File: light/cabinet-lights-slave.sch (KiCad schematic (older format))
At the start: 14 parts, among them J1 CONN_01x03, J2 CONN_01x03, J3 CONN_01x03, J4 CONN_01x03, Q1 Q_PMOS_GDS, U1 MCP6001

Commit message: More schematic wrangling
Parts for light module
Initial PCB for light module
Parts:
- removed D1, D2, D3: LED, symbol LED
- removed Q1: Q_PMOS_GDS, symbol Q_PMOS_GDS
- removed R3, R4: R, symbol R
- removed U1: MCP6001, symbol MCP6001
- added D1, D2, D3: XLAMP-MX-3, parts:XLAMP-MX-3, symbol XLAMP-MX-3
- added HS1: HEATSINK, parts:25mm_heatsink, symbol TESTPAD
- added OP?1: MIC6211, agg:SOT-23-5, symbol MIC6211
- added Q1: NX7002AK, agg:SOT-23, symbol Q_NMOS_GSD
- added Q2: NTR1P02T1G, agg:SOT-23, symbol Q_PMOS_GSD
- added R6: 1k, agg:0603, symbol R
- J1: value CONN_01x03 -> NORTH; footprint (none) -> parts:S3D-XH-A; Farnell (none) -> 1516290
- J2: value CONN_01x03 -> EAST; footprint (none) -> parts:S3D-XH-A; Farnell (none) -> 1516290
- J3: value CONN_01x03 -> SOUTH; footprint (none) -> parts:S3D-XH-A; Farnell (none) -> 1516290
- J4: value CONN_01x03 -> WEST; footprint (none) -> parts:S3D-XH-A; Farnell (none) -> 1516290
- R1: value 9k -> 9k9; footprint (none) -> agg:0603
- R2: value 1k -> 100R; footprint (none) -> agg:0603
- R5: value R -> 0R24; footprint (none) -> agg:0603; Farnell (none) -> 2328092
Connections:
- net labels added: DIM/100
- net labels removed: DIM/10
- wire segments 22 -> 23

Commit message: Models for LED and JST conn, slight PCB shuffle
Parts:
- J1, J2, J3, J4: footprint parts:S3D-XH-A -> parts:S3B-XH-A
- renumbered R5 to R3, R6 to R4
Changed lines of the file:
@@
 F 0 "J1" H 4231 2673 50  0001 C CNN
 F 1 "NORTH" V 4100 2450 50  0000 C CNN
-F 2 "parts:S3D-XH-A" H 4200 2550 50  0001 C CNN
+F 2 "parts:S3B-XH-A" H 4200 2550 50  0001 C CNN
 F 3 "http://www.farnell.com/datasheets/5448.pdf" H 4200 2550 50  0001 C CNN
 F 4 "1516290" H 4200 2550 60  0001 C CNN "Farnell"
@@
 $EndComp
 $Comp
-L R R5
+L R R3
 U 1 1 577A3D2F
 P 6400 3625
-F 0 "R5" H 6470 3671 50  0001 L CNN
+F 0 "R3" H 6470 3671 50  0001 L CNN
 F 1 "0R24" V 6400 3625 50  0000 C CNN
 F 2 "agg:0603" V 6330 3625 50  0001 C CNN
@@
 $EndComp
 $Comp
-L R R6
+L R R4
 U 1 1 577B9A14
 P 6100 2500
-F 0 "R6" V 5893 2500 50  0001 C CNN
+F 0 "R4" V 5893 2500 50  0001 C CNN
 F 1 "1k" V 6100 2500 50  0000 C CNN
 F 2 "agg:0603" V 6030 2500 50  0001 C CNN
@@
 F 0 "J2" H 4231 3023 50  0001 C CNN
 F 1 "EAST" V 4100 2800 50  0000 C CNN
-F 2 "parts:S3D-XH-A" H 4200 2900 50  0001 C CNN
+F 2 "parts:S3B-XH-A" H 4200 2900 50  0001 C CNN
 F 3 "http://www.farnell.com/datasheets/5448.pdf" H 4200 2900 50  0001 C CNN
 F 4 "1516290" H 4200 2900 60  0001 C CNN "Farnell"
@@
 F 0 "J3" H 4231 3373 50  0001 C CNN
 F 1 "SOUTH" V 4100 3150 50  0000 C CNN
-F 2 "parts:S3D-XH-A" H 4200 3250 50  0001 C CNN
+F 2 "parts:S3B-XH-A" H 4200 3250 50  0001 C CNN
 F 3 "http://www.farnell.com/datasheets/5448.pdf" H 4200 3250 50  0001 C CNN
 F 4 "1516290" H 4200 3250 60  0001 C CNN "Farnell"
@@
 F 0 "J4" H 4231 3723 50  0001 C CNN
 F 1 "WEST" V 4100 3500 50  0000 C CNN
-F 2 "parts:S3D-XH-A" H 4200 3600 50  0001 C CNN
+F 2 "parts:S3B-XH-A" H 4200 3600 50  0001 C CNN
 F 3 "http://www.farnell.com/datasheets/5448.pdf" H 4200 3600 50  0001 C CNN
 F 4 "1516290" H 4200 3600 60  0001 C CNN "Farnell"

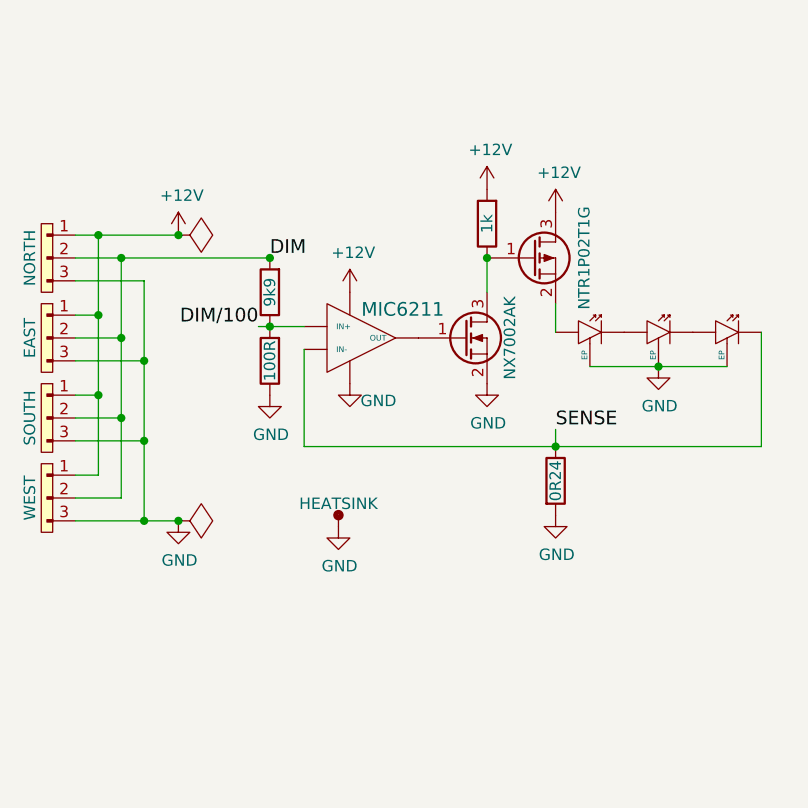
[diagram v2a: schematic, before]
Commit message: Tweak to use BJT transistor
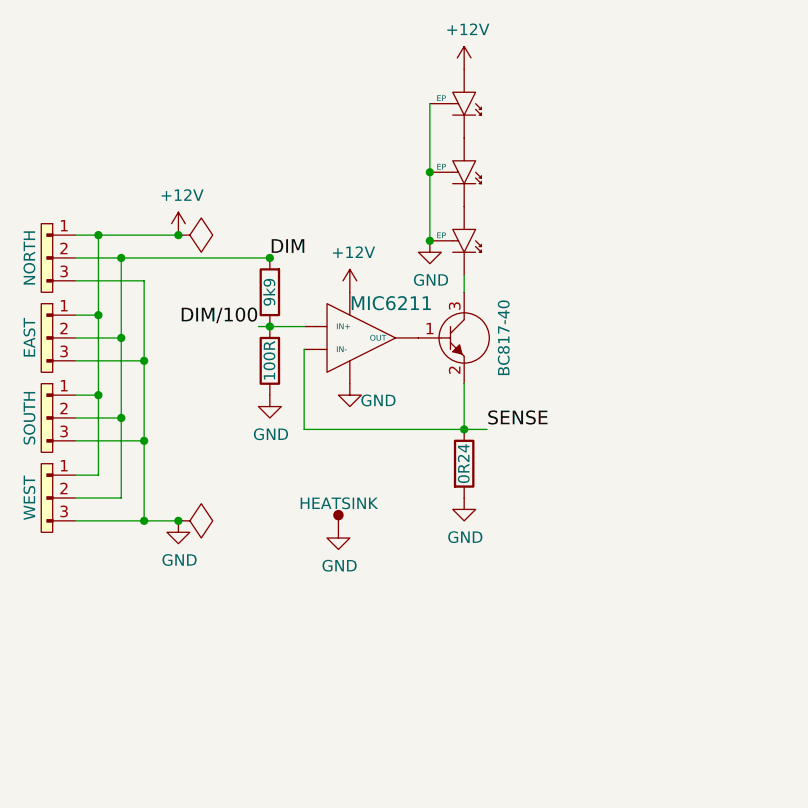
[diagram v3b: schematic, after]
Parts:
- removed Q1: NX7002AK, agg:SOT-23, symbol Q_NMOS_GSD
- removed Q2: NTR1P02T1G, agg:SOT-23, symbol Q_PMOS_GSD
- removed R4: 1k, agg:0603, symbol R
- added Q1: BC817-40, agg:SOT-23, symbol NPN
- renumbered OP?1 to OP1
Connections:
- net +12V: now also D1.2
- net SENSE: now also Q1.2 (E); no longer D3.1
- net at OP1.1 (OUT): now also Q1.1 (B)
- new net: D3.1, Q1.3 (C)
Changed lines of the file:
@@
 $EndComp
 $Comp
-L +12V #PWR01
+L +12V #PWR1
 U 1 1 577A3A01
 P 4750 2550
-F 0 "#PWR01" H 4750 2400 50  0001 C CNN
+F 0 "#PWR1" H 4750 2400 50  0001 C CNN
 F 1 "+12V" H 4765 2723 50  0000 C CNN
 F 2 "" H 4750 2550 50  0000 C CNN
@@
 $EndComp
 $Comp
-L PWR_FLAG #FLG02
+L PWR_FLAG #FLG1
 U 1 1 577A3A92
 P 4750 2550
-F 0 "#FLG02" H 4750 2645 50  0001 C CNN
+F 0 "#FLG1" H 4750 2645 50  0001 C CNN
 F 1 "PWR_FLAG" V 4750 2728 50  0001 L CNN
 F 2 "" H 4750 2550 50  0000 C CNN
@@
 $EndComp
 $Comp
-L +12V #PWR03
+L +12V #PWR5
 U 1 1 577A3BB5
 P 5500 2800
-F 0 "#PWR03" H 5500 2650 50  0001 C CNN
+F 0 "#PWR5" H 5500 2650 50  0001 C CNN
 F 1 "+12V" H 5515 2973 50  0000 C CNN
 F 2 "" H 5500 2800 50  0000 C CNN
@@
 $EndComp
 $Comp
-L GND #PWR04
+L GND #PWR6
 U 1 1 577A3BC0
 P 5500 3200
-F 0 "#PWR04" H 5500 2950 50  0001 C CNN
+F 0 "#PWR6" H 5500 2950 50  0001 C CNN
 F 1 "GND" H 5625 3125 50  0000 C CNN
 F 2 "" H 5500 3200 50  0000 C CNN
@@
 L R R3
 U 1 1 577A3D2F
-P 6400 3625
-F 0 "R3" H 6470 3671 50  0001 L CNN
-F 1 "0R24" V 6400 3625 50  0000 C CNN
-F 2 "agg:0603" V 6330 3625 50  0001 C CNN
-F 3 "http://www.farnell.com/datasheets/2004190.pdf" H 6400 3625 50  0001 C CNN
-F 4 "2328092" H 6400 3625 60  0001 C CNN "Farnell"
-	1    6400 3625
-	1    0    0    -1
-$EndComp
-$Comp
-L +12V #PWR05
+P 6000 3550
+F 0 "R3" H 6070 3596 50  0001 L CNN
+F 1 "0R24" V 6000 3550 50  0000 C CNN
+F 2 "agg:0603" V 5930 3550 50  0001 C CNN
+F 3 "http://www.farnell.com/datasheets/2004190.pdf" H 6000 3550 50  0001 C CNN
+F 4 "2328092" H 6000 3550 60  0001 C CNN "Farnell"
+	1    6000 3550
+	1    0    0    -1
+$EndComp
+$Comp
+L +12V #PWR8
 U 1 1 577A3FBE
-P 6400 2450
-F 0 "#PWR05" H 6400 2300 50  0001 C CNN
-F 1 "+12V" H 6415 2623 50  0000 C CNN
-F 2 "" H 6400 2450 50  0000 C CNN
-F 3 "" H 6400 2450 50  0000 C CNN
-	1    6400 2450
-	1    0    0    -1
-$EndComp
-$Comp
-L GND #PWR06
+P 6000 1825
+F 0 "#PWR8" H 6000 1675 50  0001 C CNN
+F 1 "+12V" H 6015 1998 50  0000 C CNN
+F 2 "" H 6000 1825 50  0000 C CNN
+F 3 "" H 6000 1825 50  0000 C CNN
+	1    6000 1825
+	1    0    0    -1
+$EndComp
+$Comp
+L GND #PWR9
 U 1 1 577A3FD8
-P 6400 3775
-F 0 "#PWR06" H 6400 3525 50  0001 C CNN
-F 1 "GND" H 6405 3602 50  0000 C CNN
-F 2 "" H 6400 3775 50  0000 C CNN
-F 3 "" H 6400 3775 50  0000 C CNN
-	1    6400 3775
+P 6000 3700
+F 0 "#PWR9" H 6000 3450 50  0001 C CNN
+F 1 "GND" H 6005 3527 50  0000 C CNN
+F 2 "" H 6000 3700 50  0000 C CNN
+F 3 "" H 6000 3700 50  0000 C CNN
+	1    6000 3700
 	1    0    0    -1
 $EndComp
@@
 	4300 3800 4750 3800
 $Comp
-L GND #PWR07
+L GND #PWR2
 U 1 1 577A3A2D
 P 4750 3800
-F 0 "#PWR07" H 4750 3550 50  0001 C CNN
+F 0 "#PWR2" H 4750 3550 50  0001 C CNN
 F 1 "GND" H 4755 3627 50  0000 C CNN
 F 2 "" H 4750 3800 50  0000 C CNN
@@
 $EndComp
 $Comp
-L PWR_FLAG #FLG08
+L PWR_FLAG #FLG2
 U 1 1 577A3AA4
 P 4750 3800
-F 0 "#FLG08" H 4750 3895 50  0001 C CNN
+F 0 "#FLG2" H 4750 3895 50  0001 C CNN
 F 1 "PWR_FLAG" V 4750 3978 50  0001 L CNN
 F 2 "" H 4750 3800 50  0000 C CNN
@@
 $EndComp
 $Comp
-L GND #PWR09
+L GND #PWR3
 U 1 1 577A5F6E
 P 5150 3250
-F 0 "#PWR09" H 5150 3000 50  0001 C CNN
+F 0 "#PWR3" H 5150 3000 50  0001 C CNN
 F 1 "GND" H 5155 3077 50  0000 C CNN
 F 2 "" H 5150 3250 50  0000 C CNN
@@
 Connection ~ 5150 2950
 Connection ~ 5150 2650
-Text Label 6400 3400 0    60   ~ 0
+Text Label 6100 3400 0    60   ~ 0
 SENSE
-Connection ~ 6400 3475
-$Comp
-L GND #PWR010
-U 1 1 577B9A09
-P 6100 3200
-F 0 "#PWR010" H 6100 2950 50  0001 C CNN
-F 1 "GND" H 6105 3027 50  0000 C CNN
-F 2 "" H 6100 3200 50  0000 C CNN
-F 3 "" H 6100 3200 50  0000 C CNN
-	1    6100 3200
-	1    0    0    -1
-$EndComp
-$Comp
-L R R4
-U 1 1 577B9A14
-P 6100 2500
-F 0 "R4" V 5893 2500 50  0001 C CNN
-F 1 "1k" V 6100 2500 50  0000 C CNN
-F 2 "agg:0603" V 6030 2500 50  0001 C CNN
-F 3 "" H 6100 2500 50  0000 C CNN
-	1    6100 2500
-	-1   0    0    1
-$EndComp
-$Comp
-L +12V #PWR011
-U 1 1 577B9A1F
-P 6100 2350
-F 0 "#PWR011" H 6100 2200 50  0001 C CNN
-F 1 "+12V" H 6115 2523 50  0000 C CNN
-F 2 "" H 6100 2350 50  0000 C CNN
-F 3 "" H 6100 2350 50  0000 C CNN
-	1    6100 2350
-	1    0    0    -1
-$EndComp
-$Comp
-L Q_PMOS_GSD Q2
-U 1 1 577B9E2C
-P 6300 2650
-F 0 "Q2" H 6491 2696 50  0001 L CNN
-F 1 "NTR1P02T1G" V 6525 2650 50  0000 C CNN
-F 2 "agg:SOT-23" H 6500 2750 50  0001 C CNN
-F 3 "http://www.farnell.com/datasheets/1708311.pdf" H 6300 2650 50  0001 C CNN
-F 4 "2317617" H 6300 2650 60  0001 C CNN "Farnell"
-	1    6300 2650
-	1    0    0    -1
-$EndComp
-$Comp
-L Q_NMOS_GSD Q1
-U 1 1 577BA518
-P 6000 3000
-F 0 "Q1" H 6191 3046 50  0001 L CNN
-F 1 "NX7002AK" V 6200 3000 50  0000 C CNN
-F 2 "agg:SOT-23" H 6200 3100 50  0001 C CNN
-F 3 "http://www.farnell.com/datasheets/1968065.pdf" H 6000 3000 50  0001 C CNN
-	1    6000 3000
-	1    0    0    -1
-$EndComp
-Wire Wire Line
-	6100 2800 6100 2650
-Connection ~ 6100 2650
-$Comp
-L MIC6211 OP?1
+Connection ~ 6000 3400
+$Comp
+L MIC6211 OP1
 U 1 1 577BB3FE
 P 5500 3000
-F 0 "OP?1" H 5575 2900 60  0001 L CNN
-F 1 "MIC6211" H 5550 3125 60  0000 L CNN
+F 0 "OP1" H 5575 2900 60  0001 L CNN
+F 1 "MIC6211" H 5500 3150 60  0000 L CNN
 F 2 "agg:SOT-23-5" H 5550 3000 60  0001 C CNN
 F 3 "http://www.farnell.com/datasheets/94475.pdf" H 5550 3000 60  0001 C CNN
@@
 Wire Wire Line
 	5100 2950 5300 2950
-Wire Wire Line
-	5300 3050 5300 3475
 $Comp
 L XLAMP-MX-3 D1
 U 1 1 577BB7DA
-P 6550 2975
-F 0 "D1" H 6425 2900 60  0001 C CNN
-F 1 "XLAMP-MX-3" H 6450 3100 60  0001 C CNN
-F 2 "parts:XLAMP-MX-3" H 6450 2675 60  0001 C CNN
-F 3 "http://www.farnell.com/datasheets/1810580.pdf" H 6550 2775 60  0001 C CNN
-F 4 "1855576" H 6650 2875 60  0001 C CNN "Farnell"
-	1    6550 2975
-	-1   0    0    1
+P 6000 1975
+F 0 "D1" H 5875 1900 60  0001 C CNN
+F 1 "XLAMP-MX-3" H 5900 2100 60  0001 C CNN
+F 2 "parts:XLAMP-MX-3" H 5900 1675 60  0001 C CNN
+F 3 "http://www.farnell.com/datasheets/1810580.pdf" H 6000 1775 60  0001 C CNN
+F 4 "1855576" H 6100 1875 60  0001 C CNN "Farnell"
+	1    6000 1975
+	0    -1   -1   0
 $EndComp
 $Comp
 L XLAMP-MX-3 D2
 U 1 1 577BB9A5
-P 6850 2975
-F 0 "D2" H 6725 2900 60  0001 C CNN
-F 1 "XLAMP-MX-3" H 6750 3100 60  0001 C CNN
-F 2 "parts:XLAMP-MX-3" H 6750 2675 60  0001 C CNN
-F 3 "http://www.farnell.com/datasheets/1810580.pdf" H 6850 2775 60  0001 C CNN
-F 4 "1855576" H 6950 2875 60  0001 C CNN "Farnell"
-	1    6850 2975
-	-1   0    0    1
+P 6000 2275
+F 0 "D2" H 5875 2200 60  0001 C CNN
+F 1 "XLAMP-MX-3" H 5900 2400 60  0001 C CNN
+F 2 "parts:XLAMP-MX-3" H 5900 1975 60  0001 C CNN
+F 3 "http://www.farnell.com/datasheets/1810580.pdf" H 6000 2075 60  0001 C CNN
+F 4 "1855576" H 6100 2175 60  0001 C CNN "Farnell"
+	1    6000 2275
+	0    -1   -1   0
 $EndComp
 $Comp
 L XLAMP-MX-3 D3
 U 1 1 577BB9B2
-P 7150 2975
-F 0 "D3" H 7025 2900 60  0001 C CNN
-F 1 "XLAMP-MX-3" H 7050 3100 60  0001 C CNN
-F 2 "parts:XLAMP-MX-3" H 7050 2675 60  0001 C CNN
-F 3 "http://www.farnell.com/datasheets/1810580.pdf" H 7150 2775 60  0001 C CNN
-F 4 "1855576" H 7250 2875 60  0001 C CNN "Farnell"
-	1    7150 2975
-	-1   0    0    1
-$EndComp
-$Comp
-L GND #PWR012
+P 6000 2575
+F 0 "D3" H 5875 2500 60  0001 C CNN
+F 1 "XLAMP-MX-3" H 5900 2700 60  0001 C CNN
+F 2 "parts:XLAMP-MX-3" H 5900 2275 60  0001 C CNN
+F 3 "http://www.farnell.com/datasheets/1810580.pdf" H 6000 2375 60  0001 C CNN
+F 4 "1855576" H 6100 2475 60  0001 C CNN "Farnell"
+	1    6000 2575
+	0    -1   -1   0
+$EndComp
+$Comp
+L GND #PWR7
 U 1 1 577BB9BE
-P 6850 3125
-F 0 "#PWR012" H 6850 2875 50  0001 C CNN
-F 1 "GND" H 6855 2952 50  0000 C CNN
-F 2 "" H 6850 3125 50  0000 C CNN
-F 3 "" H 6850 3125 50  0000 C CNN
-	1    6850 3125
-	1    0    0    -1
-$EndComp
-Wire Wire Line
-	6550 3125 7150 3125
-Connection ~ 6850 3125
-Wire Wire Line
-	6400 2850 6400 2975
-Wire Wire Line
-	5300 3475 7300 3475
-Wire Wire Line
-	7300 3475 7300 2975
-Wire Wire Line
-	6400 3400 6400 3475
-$Comp
-L GND #PWR013
+P 5850 2575
+F 0 "#PWR7" H 5850 2325 50  0001 C CNN
+F 1 "GND" H 5855 2402 50  0000 C CNN
+F 2 "" H 5850 2575 50  0000 C CNN
+F 3 "" H 5850 2575 50  0000 C CNN
+	1    5850 2575
+	1    0    0    -1
+$EndComp
+Wire Wire Line
+	5850 1975 5850 2575
+Connection ~ 5850 2275
+$Comp
+L GND #PWR4
 U 1 1 577BBDBD
 P 5450 3825
-F 0 "#PWR013" H 5450 3575 50  0001 C CNN
+F 0 "#PWR4" H 5450 3575 50  0001 C CNN
 F 1 "GND" H 5455 3652 50  0000 C CNN
 F 2 "" H 5450 3825 50  0000 C CNN
@@
 	1    0    0    -1
 $EndComp
+Connection ~ 5850 2575
+$Comp
+L NPN Q1
+U 1 1 577D708B
+P 6000 3000
+F 0 "Q1" H 6138 3046 50  0001 L CNN
+F 1 "BC817-40" V 6175 3000 50  0000 C CNN
+F 2 "agg:SOT-23" H 6030 2920 50  0001 C CNN
+F 3 "http://www.farnell.com/datasheets/1702498.pdf" H 6130 3020 50  0001 C CNN
+F 4 "1798081" H 6000 3000 60  0001 C CNN "Farnell"
+	1    6000 3000
+	1    0    0    -1
+$EndComp
+Wire Wire Line
+	6000 2725 6000 2800
+Wire Wire Line
+	6100 3400 5300 3400
+Wire Wire Line
+	5300 3400 5300 3050
+Wire Wire Line
+	6000 3200 6000 3400
 $EndSCHEMATC

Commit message: Mounting holes, some track shenanigans
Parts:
- added X1, X2, X3, X4: MOUNT, Mounting_Holes:MountingHole_2.7mm_M2.5, symbol PART
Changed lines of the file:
@@
 Wire Wire Line
 	6000 3200 6000 3400
+$Comp
+L PART X4
+U 1 1 577DA12A
+P 6925 4200
+F 0 "X4" H 7453 4296 50  0001 L CNN
+F 1 "MOUNT" H 7175 4250 50  0000 C CNN
+F 2 "Mounting_Holes:MountingHole_2.7mm_M2.5" H 6925 4200 50  0001 C CNN
+F 3 "" H 6925 4200 50  0001 C CNN
+	1    6925 4200
+	1    0    0    -1
+$EndComp
+$Comp
+L PART X3
+U 1 1 577DA2D1
+P 6925 3975
+F 0 "X3" H 7453 4071 50  0001 L CNN
+F 1 "MOUNT" H 7175 4025 50  0000 C CNN
+F 2 "Mounting_Holes:MountingHole_2.7mm_M2.5" H 6925 3975 50  0001 C CNN
+F 3 "" H 6925 3975 50  0001 C CNN
+	1    6925 3975
+	1    0    0    -1
+$EndComp
+$Comp
+L PART X2
+U 1 1 577DA2DC
+P 6925 3750
+F 0 "X2" H 7453 3846 50  0001 L CNN
+F 1 "MOUNT" H 7175 3800 50  0000 C CNN
+F 2 "Mounting_Holes:MountingHole_2.7mm_M2.5" H 6925 3750 50  0001 C CNN
+F 3 "" H 6925 3750 50  0001 C CNN
+	1    6925 3750
+	1    0    0    -1
+$EndComp
+$Comp
+L PART X1
+U 1 1 577DA2E7
+P 6925 3525
+F 0 "X1" H 7453 3621 50  0001 L CNN
+F 1 "MOUNT" H 7175 3575 50  0000 C CNN
+F 2 "Mounting_Holes:MountingHole_2.7mm_M2.5" H 6925 3525 50  0001 C CNN
+F 3 "" H 6925 3525 50  0001 C CNN
+	1    6925 3525
+	1    0    0    -1
+$EndComp
 $EndSCHEMATC
